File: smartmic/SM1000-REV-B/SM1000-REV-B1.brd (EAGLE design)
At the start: 65 x 90 mm, 173 parts, among them CN1 HDR100-3, CN10 MJ-3523-SMT, CN11 HDR100-3, CN12 DF11-16DS, CN2 MOLEX-MINI-B-SMT, CN3 RASM712PX, CN4 RJ-45, CN5 MJ-3523-SMT, CN6 MJ-3523-SMT, CN7 MJ-3523-SMT, CN8 MJ-3523-SMT, CN9 MJ-3523-SMT, J1 JMP-2PIN, J2 JMP-2PIN, J3 JMP-2PIN, J4 JMP-2PIN, J5 JMP-2PIN, J7 JMP-2PIN, P1 TPAD50, P10 TPAD50, P11 TPAD50, P12 TPAD50, P13 TPAD50, P14 TPAD50, P15 TPAD50, P16 TPAD50, P17 TPAD50, P18 TPAD50, P19 TPAD50, P2 TPAD50, P20 TPAD50, P3 TPAD50, P4 TPAD50, P5 TPAD50, P6 TPAD50, P7 TPAD50, P8 TPAD50, P9 TPAD50, SW1 SW-BOURNS-7914S, SW2 SW-BOURNS-7914S, SW3 DPDT, SW4 SW-BOURNS-7914S, T1 SM-LP-5001, T2 SM-LP-5001, U1 STM32F405, U2 LD3985M33R, U3 STMPS2141, U4 EMIF02-USB03F2, U5 TPS54329E, U6 LMV341, U7 LMV341, U8 LM386M-1, U9 LMV341

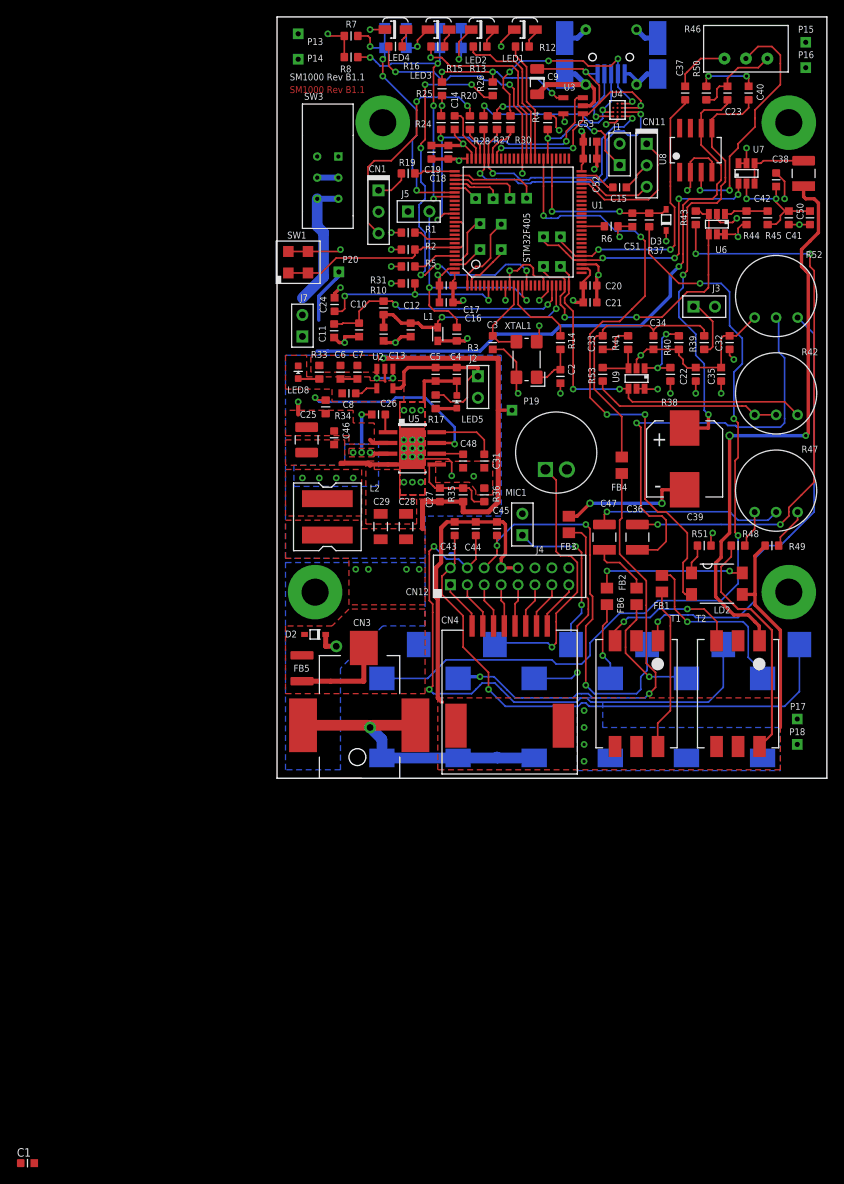
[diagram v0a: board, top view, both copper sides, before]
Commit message: 
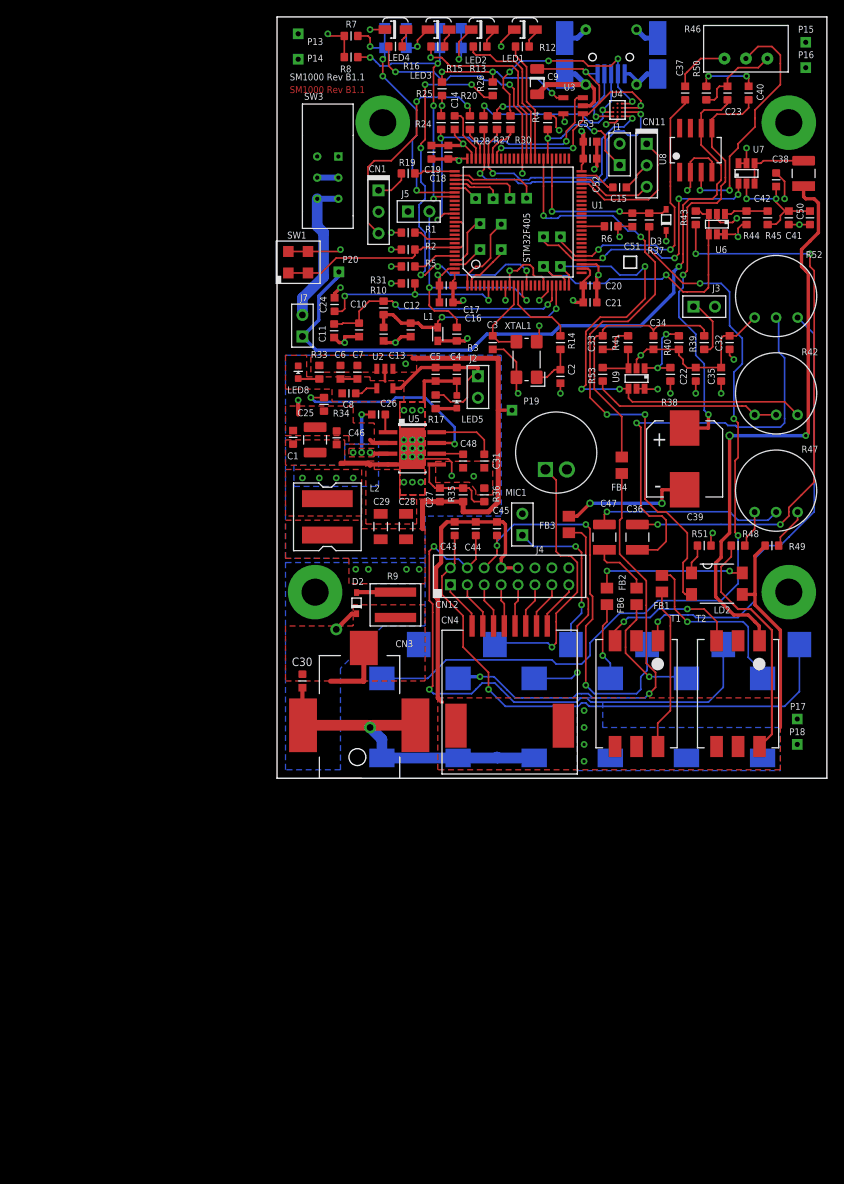
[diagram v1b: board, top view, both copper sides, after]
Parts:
- removed FB5: FB1210, _RoweTel:FE1210
- added C30: 10nF,25V, AA-ipc-7351-capacitor:CAPC1608X92N
- added R9: 10,5%,1218, SM1000:RCL1218
- moved C1 91.4 mm to (1.90, 40.3), turned to 90 degrees
- moved D2 6.14 mm to (9.40, 20.7), turned to 90 degrees
- moved C25 1.00 mm to (4.50, 40.0)
- moved R34 0.36 mm to (5.55, 44.2)
- moved C46 0.30 mm to (7.05, 40.2)
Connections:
- net GND: now also C30.2
- net N$24: now also R9.2; no longer FB5.2
- net N$77: now also C30.1, R9.1; no longer FB5.1
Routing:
- net AIN2: track 44.0 -> 60.4 mm, vias 2 -> 3
- net GND: track 245.4 -> 251.1 mm
- net +VIN: track 95.4 -> 100.8 mm
- net +5V: track 101.2 -> 96.6 mm, vias 8 -> 6
- net N$24: track 0.00 -> 4.62 mm
- net N$77: track 11.2 -> 7.86 mm
- net N$70: track 15.6 -> 17.6 mm
- net +VEXT: track 76.5 -> 74.8 mm
- net !CPPT!: track 74.9 -> 76.5 mm
- net VDD: track 79.2 -> 80.4 mm
- net AIN1: track 37.3 -> 36.1 mm, vias 2 -> 1
- net +3.3V: track 20.8 -> 19.8 mm
- net DAC1_OUT: track 32.8 -> 33.6 mm
- net N$42: track 23.9 -> 24.6 mm
- added copper zone on layer 1, net N$77
- removed copper zone on layer 1, net N$24

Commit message: The latest SM1000-REV-B1 PCB design - RGB
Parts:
- added R11: 100,1%, AA-ipc-7351-resistor:RESC1608X55N
- C34: value 100pF,50V -> 1nF,50V
- moved P14 3.04 mm to (3.00, 88.0)
- moved R8 2.69 mm to (7.75, 87.8), turned to 270 degrees
- moved P13 2.55 mm to (3.00, 85.5)
- moved FB4 1.52 mm to (40.5, 35.5)
- moved R7 1.50 mm to (10.2, 87.8), turned to 270 degrees
- moved R26 1.00 mm to (24.5, 81.5)
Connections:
- net N$11 renamed PE0
- net N$13 renamed PE1
- net N$14 renamed PE2
- net N$15 renamed PE3
- removed net !BACK!: R8.1, SW4.3, SW4.4, U1.82
- removed net !SELECT!: R7.1, SW2.3, SW2.4, U1.81
- new net BACK: R8.2, SW4.1, SW4.2, U1.82
- new net N$26: FB4.2, R11.1
- new net SELECT: R7.2, SW2.1, SW2.2, U1.81
- net GND: now also R7.1, R8.1; no longer SW2.1, SW2.2, SW4.1, SW4.2
- net N$25: now also R11.2; no longer FB4.2
- net VDD: now also SW2.3, SW2.4, SW4.3, SW4.4; no longer R7.2, R8.2
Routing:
- net BACK: track 0.00 -> 40.4 mm, vias 0 -> 2
- net !BACK!: track 33.1 -> 0.00 mm, vias 4 -> 0
- net SELECT: track 0.00 -> 31.2 mm, vias 0 -> 2
- net !SELECT!: track 30.3 -> 0.00 mm, vias 4 -> 0
- net GND: track 251.1 -> 233.8 mm, vias 48 -> 46
- net VDD: track 80.4 -> 89.5 mm, vias 24 -> 27
- net OTG_PWR_ON: track 48.4 -> 45.8 mm, vias 6 -> 4
- net N$25: track 31.4 -> 29.0 mm
- net N$31: track 18.0 -> 15.6 mm, vias 3 -> 2
- net N$26: track 0.00 -> 2.23 mm
- net N$76: track 52.5 -> 50.9 mm
- net N$6: track 27.6 -> 29.0 mm
- net N$60: track 31.9 -> 31.4 mm
- net !CPPT!: track 76.5 -> 77.0 mm
- net LED-RT: track 23.1 -> 22.7 mm, vias 1 -> 0
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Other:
- board text added: "SM1000 Rev B1"
- board text removed: "SM1000 Rev B1.1"
